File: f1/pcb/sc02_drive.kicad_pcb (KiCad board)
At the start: 4 copper layers, 65 x 70 mm, 84 parts, among them J1 BAT 3S, J10 LICHTEN, J2 MOTOR 1, J3 MOTOR 2, J4 SERVO, J5 HALL, J6 ZONNEPANEEL, J7 I2C, J8 USB-C, J9 PI 4, Q1 AOD4185, Q2 2N7002, Q3 2N7002, Q4 AO3400A, SW1 RESET, SW2 BOOT, U1 TPS54560B, U10 USBLC6-2SC6, U2 AMS1117-3.3, U3 ESP32-S3-WROOM-1-N16R8, U4 DRV8871, U5 DRV8871, U6 INA226

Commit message: SC-02 floor board v2: the whole floor is the PCB (XT60, fuse, ELRS RP2 pads, Pi UART, USB-C at the edge); body gets a USB-C opening
Co-Authored-By: Claude Opus 5.5 <noreply@anthropic.com>
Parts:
- removed Q2, Q3: 2N7002, sc02:SOT-23
- removed R14, R15: 100k, sc02:R_0603_1608Metric
- added F1: 10A, sc02:R_2512_6332Metric, F.Cu at (216.5, 47.0)
- added H10: 3.2, sc02:Hole_3.2mm, F.Cu at (357.0, 89.0)
- added H11: 3.2, sc02:Hole_3.2mm, F.Cu at (395.0, 111.0)
- added H12: 3.2, sc02:Hole_3.2mm, F.Cu at (395.0, 89.0)
- added H13: 3.2, sc02:Hole_3.2mm, F.Cu at (405.0, 114.0)
- added H14: 3.2, sc02:Hole_3.2mm, F.Cu at (405.0, 86.0)
- added H15: 2.6, sc02:Hole_2.6mm, F.Cu at (112.2, 130.5)
- added H16: 2.6, sc02:Hole_2.6mm, F.Cu at (112.2, 100.0)
- added H17: 2.6, sc02:Hole_2.6mm, F.Cu at (112.2, 69.5)
- added H18: 3.2, sc02:Hole_3.2mm, F.Cu at (189.0, 130.0)
- added H19: 3.2, sc02:Hole_3.2mm, F.Cu at (189.0, 70.0)
- added H20: 3.2, sc02:Hole_3.2mm, F.Cu at (255.0, 130.0)
- added H21: 3.2, sc02:Hole_3.2mm, F.Cu at (255.0, 70.0)
- added H22: 3.2, sc02:Hole_3.2mm, F.Cu at (266.5, 100.0)
- added H23: 3.2, sc02:Hole_3.2mm, F.Cu at (324.5, 100.0)
- added H24: 3.2, sc02:Hole_3.2mm, F.Cu at (198.0, 39.5)
- added H25: 3.2, sc02:Hole_3.2mm, F.Cu at (198.0, 160.5)
- added H26: 3.2, sc02:Hole_3.2mm, F.Cu at (290.0, 40.0)
- added H27: 3.2, sc02:Hole_3.2mm, F.Cu at (290.0, 160.0)
- added H28: 3.2, sc02:Hole_3.2mm, F.Cu at (110.0, 54.0)
- added H29: 3.2, sc02:Hole_3.2mm, F.Cu at (110.0, 146.0)
- added H30: 3.2, sc02:Hole_3.2mm, F.Cu at (336.0, 42.0)
- added H31: 3.2, sc02:Hole_3.2mm, F.Cu at (336.0, 158.0)
- added H32: 6.2, sc02:Hole_6.2mm, F.Cu at (227.5, 36.5)
- added H5: 3.2, sc02:Hole_3.2mm, F.Cu at (145.0, 118.0)
- added H6: 3.2, sc02:Hole_3.2mm, F.Cu at (145.0, 82.0)
- added H7: 3.2, sc02:Hole_3.2mm, F.Cu at (143.5, 44.5)
- added H8: 3.2, sc02:Hole_3.2mm, F.Cu at (156.5, 44.5)
- added H9: 3.2, sc02:Hole_3.2mm, F.Cu at (357.0, 111.0)
- added J11: SCHAKELAAR, sc02:SolderWire_2pad_P5mm_SW, F.Cu at (216.5, 38.5)
- added J12: ELRS RP2, sc02:Pads_ELRS_RX, F.Cu at (252.5, 61.0)
- added J13: 5V PI, sc02:SolderWire_2pad_P5mm_5V, F.Cu at (276.0, 61.0)
- added R29: 100, sc02:R_0603_1608Metric, F.Cu at (252.4, 56.5)
- added R30: 100, sc02:R_0603_1608Metric, F.Cu at (254.2, 56.5)
- H1, H2, H3, H4: value M2.5 -> 3.2; footprint sc02:MountingHole_2.75mm_M2.5_Pi -> sc02:Hole_3.2mm
- J1: value BAT 3S -> XT60; footprint sc02:SolderWire_2pad_P7mm_D2.2mm_BAT -> sc02:AMASS_XT60-M_1x02_P7.20mm_Vertical
- J9: value PI 4 -> PI UART; footprint sc02:PinSocket_2x20_P2.54mm_Vertical -> sc02:Pads_PI_UART; moved to F.Cu
- moved R12 140.3 mm to (257.6, 164.0)
- moved J9 139.9 mm to (265.5, 61.0), turned to 0 degrees
- moved C19 137.0 mm to (255.8, 164.0)
- moved R11 133.6 mm to (254.0, 164.0)
- moved C16 118.8 mm to (255.5, 160.0)
- moved C15 118.7 mm to (259.0, 160.0)
- moved R18 116.5 mm to (280.0, 147.5)
- moved C14 113.5 mm to (255.0, 147.0), turned to 0 degrees
- moved R26 113.2 mm to (274.0, 148.5)
- moved U2 112.9 mm to (257.5, 153.0), turned to 90 degrees
- moved J4 112.9 mm to (283.0, 139.0)
- moved Q4 110.6 mm to (274.0, 145.5)
- moved R28 110.6 mm to (282.0, 156.5)
- moved R17 110.6 mm to (257.8, 56.5), turned to 90 degrees
- moved SW1 110.4 mm to (228.6, 163.6), turned to 0 degrees
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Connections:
- J1 pad 2: VBAT_RAW -> BAT_IN
- J9 pad 1: unconnected-(J9-Pin_1-Pad1) -> GND
- J9 pad 2: V5 -> PI_TXD
- J9 pad 3: unconnected-(J9-Pin_3-Pad3) -> PI_RXD
- U3 pad 18: HALL -> unconnected-(U3-IO10-Pad18)
- U3 pad 31: unconnected-(U3-IO38-Pad31) -> HALL
- U3 pad 8: unconnected-(U3-IO15-Pad8) -> ELRS_TX
- U3 pad 9: unconnected-(U3-IO16-Pad9) -> ELRS_RX
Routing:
- net V5: track 96.8 -> 209.3 mm
- net ELRS_TX: track 0.00 -> 93.8 mm, vias 0 -> 2
- net ELRS_RX: track 0.00 -> 92.7 mm, vias 0 -> 2
- net 3V3: track 136.7 -> 207.9 mm, vias 4 -> 2
- net ESP_EN: track 106.8 -> 47.3 mm, vias 2 -> 3
- net I2C_SCL: track 80.1 -> 129.4 mm
- net ESP_RX: track 49.4 -> 96.4 mm
- net I2C_SDA: track 85.8 -> 129.1 mm
- net ESP_TX: track 53.0 -> 90.9 mm, vias 0 -> 2
- net PI_ESP_EN: track 11.8 -> 0.00 mm, vias 1 -> 0
- net PI_ESP_BOOT: track 11.3 -> 0.00 mm, vias 1 -> 0
- net VBUS_USB: track 24.7 -> 35.6 mm, vias 0 -> 2
- net M2_IN1: track 34.6 -> 45.4 mm
- net M1_IN2: track 64.0 -> 53.6 mm
- net M2_IN2: track 40.9 -> 51.2 mm, vias 4 -> 2
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- added copper zone on F.Cu, net BAT_F
- added copper zone on F.Cu, net BAT_IN
- removed copper zone on B.Cu, net V5
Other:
- board size 65 x 70 mm -> 362 x 158.6 mm
- board text added: "ELRS"
- board text added: "ELRS RP2"
- board text added: "HALL G V S"
- board text added: "PI UART"
- board text added: "RP2"
- board text added: "SC-02 DRIVE v2 floor"
- board text added: "SERVO G V S"
- board text added: "SOLAR HYPERCAR"
- board text added: "USB-C"
- board text added: "XT60 - +"
- board text removed: "CAMERA"
- board text removed: "ESP32-S3 + 2x DRV8871 v1.0"
- board text removed: "G V S"
- board text removed: "HALL"
- board text removed: "SC-02 DRIVE"
- board text removed: "SERVO"
- board text removed: "solar hypercar drive board"

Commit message: SC-02 drive board v3: compact board on standoffs, no Pi, built-in ExpressLRS receiver (ESP32-C3 + E28 SX1280, Generic C3 2400), JST-XH solar connector
Co-Authored-By: Claude Opus 5.5 <noreply@anthropic.com>
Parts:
- removed H10, H11, H12, H13, H14, H18, H19, H20, H21, H22, H23, H24, H25, H26, H27, H28, H29, H30, H31, H5, H6, H7, H8, H9: 3.2, sc02:Hole_3.2mm
- removed H15, H16, H17: 2.6, sc02:Hole_2.6mm
- removed H32: 6.2, sc02:Hole_6.2mm
- removed J13: 5V PI, sc02:SolderWire_2pad_P5mm_5V
- removed J9: PI UART, sc02:Pads_PI_UART
- removed R16, R17: 1k, sc02:R_0603_1608Metric
- added C30: 10u, sc02:C_0805_2012Metric, F.Cu at (269.0, 73.5)
- added C31: 22u, sc02:C_0805_2012Metric, F.Cu at (281.0, 76.0)
- added C32: 100n, sc02:C_0603_1608Metric, F.Cu at (269.5, 83.0)
- added C33: 10u, sc02:C_0805_2012Metric, F.Cu at (263.6, 102.6)
- added C34: 100n, sc02:C_0603_1608Metric, F.Cu at (263.6, 100.6)
- added C35: 1u, sc02:C_0603_1608Metric, F.Cu at (267.7, 91.0)
- added D10: SK6812MINI-E, sc02:LED-SMD_4P-L3.2-W2.8-LS5.9_SK6812MINI-E, F.Cu at (260.8, 109.4)
- added D9: SS14, sc02:D_SMA, F.Cu at (223.0, 73.8)
- added JP1: ZON>5V, sc02:SolderJumper-2_P1.3mm_Open_RoundedPad1.0x1.5mm, F.Cu at (229.0, 73.8)
- added R31: 10k, sc02:R_0603_1608Metric, F.Cu at (269.5, 91.0)
- added R32: 10k, sc02:R_0603_1608Metric, F.Cu at (269.5, 94.6)
- added R33: 10k, sc02:R_0603_1608Metric, F.Cu at (267.7, 94.6)
- added R34: 1k, sc02:R_0603_1608Metric, F.Cu at (265.9, 91.0)
- added R35: 1k, sc02:R_0603_1608Metric, F.Cu at (265.9, 94.6)
- added SW3: BIND, sc02:SW_Push_1P1T_NO_CK_KMR2, F.Cu at (258.6, 94.4)
- added U11: ESP32-C3-MINI-1-N4, sc02:WIFIM-SMD_ESP32-C3-MINI-1, F.Cu at (277.0, 90.0)
- added U12: E28-2G4M12S, sc02:WIRELM-SMD_E28-2G4M12S, F.Cu at (270.5, 112.0)
- added U13: AMS1117-3.3, sc02:SOT-223-3_TabPin2, F.Cu at (275.0, 76.0)
- H1, H2, H3, H4: value 3.2 -> M3
- J12: value ELRS RP2 -> RX USB; footprint sc02:Pads_ELRS_RX -> sc02:Pads_RX_USB
- J6: footprint sc02:SolderWire_2pad_P4mm_S -> sc02:JST_XH_B2B-XH-A_1x02_P2.50mm_Vertical
- moved H2 119.6 mm to (227.0, 36.0)
- moved H4 108.0 mm to (284.5, 73.0)
- moved R22 88.8 mm to (227.0, 65.0)
- moved R23 88.8 mm to (228.8, 65.0)
- moved H1 88.5 mm to (205.5, 118.5)
- moved J6 85.0 mm to (220.0, 67.0)
- moved C15 74.3 mm to (249.0, 86.4)
- moved C16 74.3 mm to (245.6, 86.4)
- moved U2 73.5 mm to (249.0, 80.0), turned to 0 degrees
- moved R26 72.0 mm to (213.5, 109.4)
- moved C14 72.0 mm to (243.0, 76.0), turned to 90 degrees
- moved R28 71.3 mm to (227.5, 110.5)
- moved J8 69.7 mm to (223.0, 118.2)
- moved U10 69.4 mm to (223.0, 109.5)
- moved Q4 68.9 mm to (213.5, 112.5)
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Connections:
- J12 pad 1: GND -> RX_USB_DM
- J12 pad 2: V5 -> RX_USB_DP
- J12 pad 3: ELRS_RX_IN -> GND
- R29 pad 1: ELRS_RX_IN -> RX_SERIAL_OUT
- R30 pad 2: ELRS_TX_OUT -> RX_SERIAL_IN
- U3 pad 10: ESP_TX -> RX_EN_CTL
- U3 pad 11: ESP_RX -> RX_BOOT_CTL
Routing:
- net ESP_RX: track 96.4 -> 0.00 mm, vias 2 -> 0
- net ESP_TX: track 90.9 -> 0.00 mm, vias 2 -> 0
- net ELRS_TX: track 93.8 -> 18.0 mm
- net 3V3_RX: track 0.00 -> 71.8 mm, vias 0 -> 2
- net ELRS_RX: track 92.7 -> 25.2 mm
- net GND: track 87.1 -> 145.2 mm, vias 152 -> 230
- net V5: track 209.3 -> 161.9 mm, vias 8 -> 13
- net RF_MOSI: track 0.00 -> 44.8 mm, vias 0 -> 2
- net I2C_SCL: track 129.4 -> 85.1 mm, vias 3 -> 4
- net 3V3: track 207.9 -> 165.5 mm, vias 2 -> 0
- net RX_USB_DM: track 0.00 -> 40.4 mm, vias 0 -> 1
- net RF_MISO: track 0.00 -> 37.5 mm, vias 0 -> 2
- net RX_USB_DP: track 0.00 -> 37.4 mm, vias 0 -> 2
- net I2C_SDA: track 129.1 -> 93.2 mm, vias 3 -> 5
- net RF_SCK: track 0.00 -> 32.6 mm, vias 0 -> 2
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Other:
- board size 362 x 158.6 mm -> 86 x 90 mm
- board text added: "BIND"
- board text added: "ELRS 2.4 GHz"
- board text added: "SC-02 DRIVE v3"
- board text added: "SOLAR HYPERCAR · DRIVE v3"
- board text added: "ZON - +"
- board text removed: "ELRS"
- board text removed: "ELRS RP2"
- board text removed: "PANEEL"
- board text removed: "PI UART"
- board text removed: "RP2"
- board text removed: "SC-02 DRIVE v2 floor"
- board text removed: "SOLAR HYPERCAR"

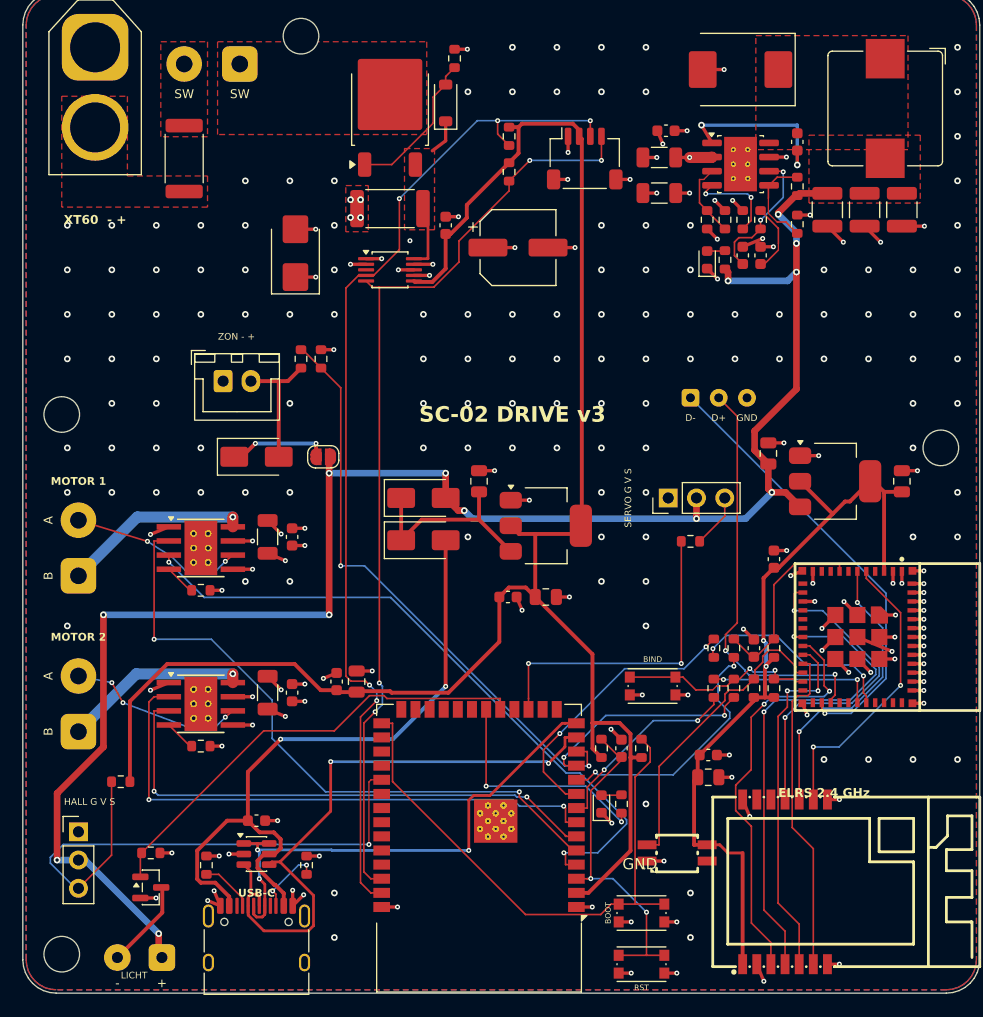
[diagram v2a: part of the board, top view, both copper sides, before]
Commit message: Drive board v3: brushless ESC output (IO4) + ESC/motor NTC (IO5) instead of 2x DRV8871
Co-Authored-By: Claude Opus 5.5 <noreply@anthropic.com>
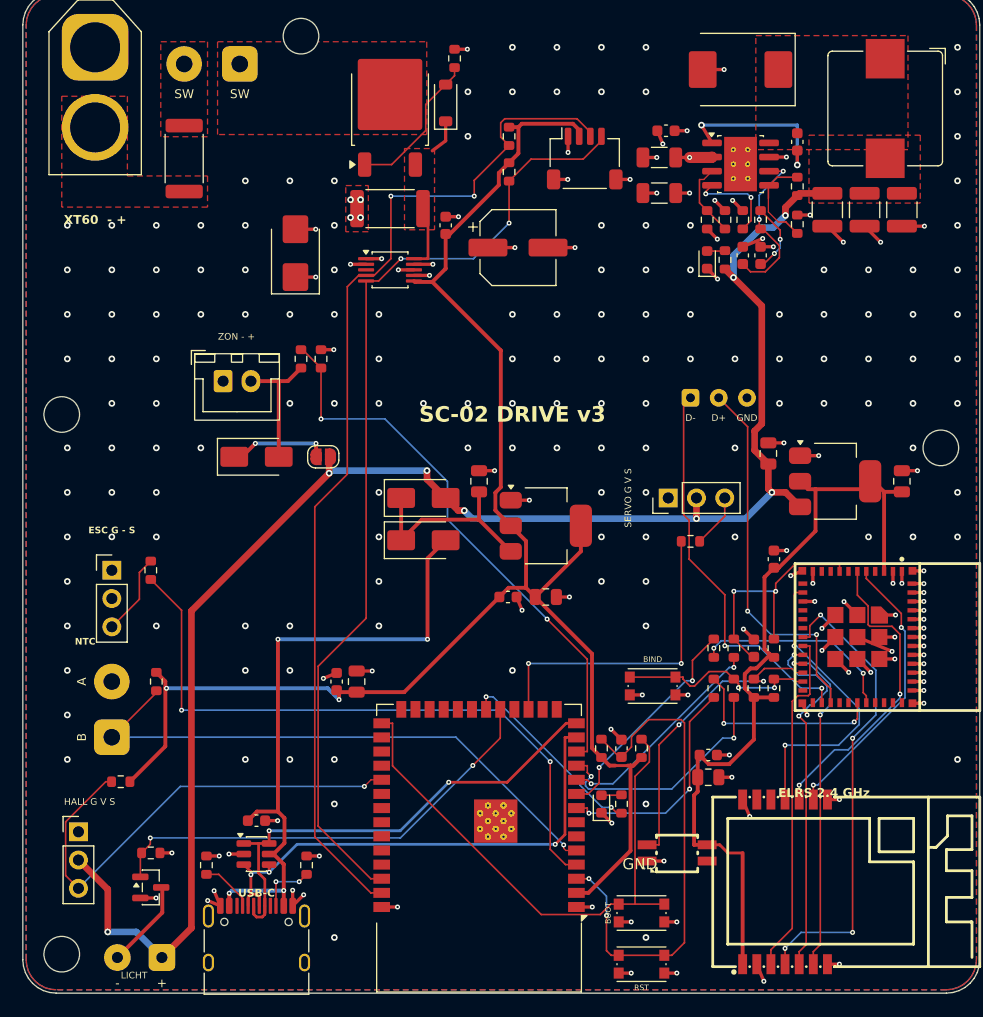
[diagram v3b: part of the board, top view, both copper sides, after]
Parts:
- removed C20, C22: 10u 25V, sc02:C_1206_3216Metric
- removed C21, C23: 100n, sc02:C_0603_1608Metric
- removed U4, U5: DRV8871, sc02:Texas_HTSOP-8-1EP_3.9x4.9mm_P1.27mm_EP2.95x4.9mm_Mask2.4x3.1mm_ThermalVias
- J2: value MOTOR 1 -> ESC; footprint sc02:SolderWire_2pad_P5mm_M -> sc02:PinHeader_1x03_P2.54mm_Vertical
- J3: value MOTOR 2 -> ESC TEMP
- R20: value 18k -> 100
- R21: value 18k -> 10k
- moved R21 7.05 mm to (214.0, 94.0), turned to 90 degrees
- moved J2 5.41 mm to (210.0, 84.0), turned to 0 degrees
- moved R20 4.85 mm to (213.5, 84.0), turned to 90 degrees
- moved J3 3.04 mm to (210.0, 94.0)
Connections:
- J2 pad 1: M1_A -> GND
- J2 pad 2: M1_B -> unconnected-(J2-Pin_2-Pad2)
- J3 pad 1: M2_A -> GND
- J3 pad 2: M2_B -> ESC_NTC
- R20 pad 1: M1_ILIM -> ESC_PWM
- R20 pad 2: GND -> ESC_SIG
- R21 pad 1: M2_ILIM -> ESC_NTC
- R21 pad 2: GND -> 3V3
- U3 pad 4: M1_IN1 -> ESC_PWM
- U3 pad 5: M1_IN2 -> ESC_NTC
- U3 pad 6: M2_IN1 -> unconnected-(U3-IO6-Pad6)
- U3 pad 7: M2_IN2 -> unconnected-(U3-IO7-Pad7)
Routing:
- net M1_IN1: track 60.5 -> 0.00 mm, vias 2 -> 0
- net ESC_PWM: track 0.00 -> 58.7 mm, vias 0 -> 2
- net M1_IN2: track 58.3 -> 0.00 mm, vias 2 -> 0
- net ESC_NTC: track 0.00 -> 52.0 mm, vias 0 -> 1
- net M2_IN2: track 50.8 -> 0.00 mm, vias 2 -> 0
- net M2_IN1: track 48.2 -> 0.00 mm, vias 2 -> 0
- net GND: track 145.2 -> 127.6 mm, vias 230 -> 234
- net M1_B: track 16.9 -> 0.00 mm, vias 1 -> 0
- net M2_B: track 16.8 -> 0.00 mm, vias 1 -> 0
- net M2_A: track 15.9 -> 0.00 mm, vias 3 -> 0
- net ESP_EN: track 30.1 -> 45.8 mm
- net M1_A: track 15.6 -> 0.00 mm, vias 2 -> 0
- net 3V3: track 165.5 -> 151.5 mm, vias 0 -> 2
- net V5: track 161.9 -> 148.1 mm, vias 13 -> 8
- net ESP_DM: track 55.8 -> 45.9 mm, vias 2 -> 3
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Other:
- board text added: "ESC G - S"
- board text added: "NTC"
- board text removed: "MOTOR 1"
- board text removed: "MOTOR 2"

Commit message: Renders: real KiCad drive PCB (matte black) + real 2S LiPo with label, leads, XT60 and balance plug; name Kobe Vanrobaeys
Co-Authored-By: Claude Opus 5.5 <noreply@anthropic.com>
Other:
- board text added: "Kobe Vanrobaeys · 2026"
- board text removed: "Kobe Van Robaeys · 2026"
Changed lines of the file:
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@@
 		)
 	)
-	(gr_text "Kobe Van Robaeys  ·  2026"
+	(gr_text "Kobe Vanrobaeys  ·  2026"
 		(at 245 64.5 0)
 		(layer "B.SilkS")
